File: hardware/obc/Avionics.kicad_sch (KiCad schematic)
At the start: 43 parts, among them J305 Conn_01x05, U103 RP2350_80QFN, Y101 Crystal_GND24_Small

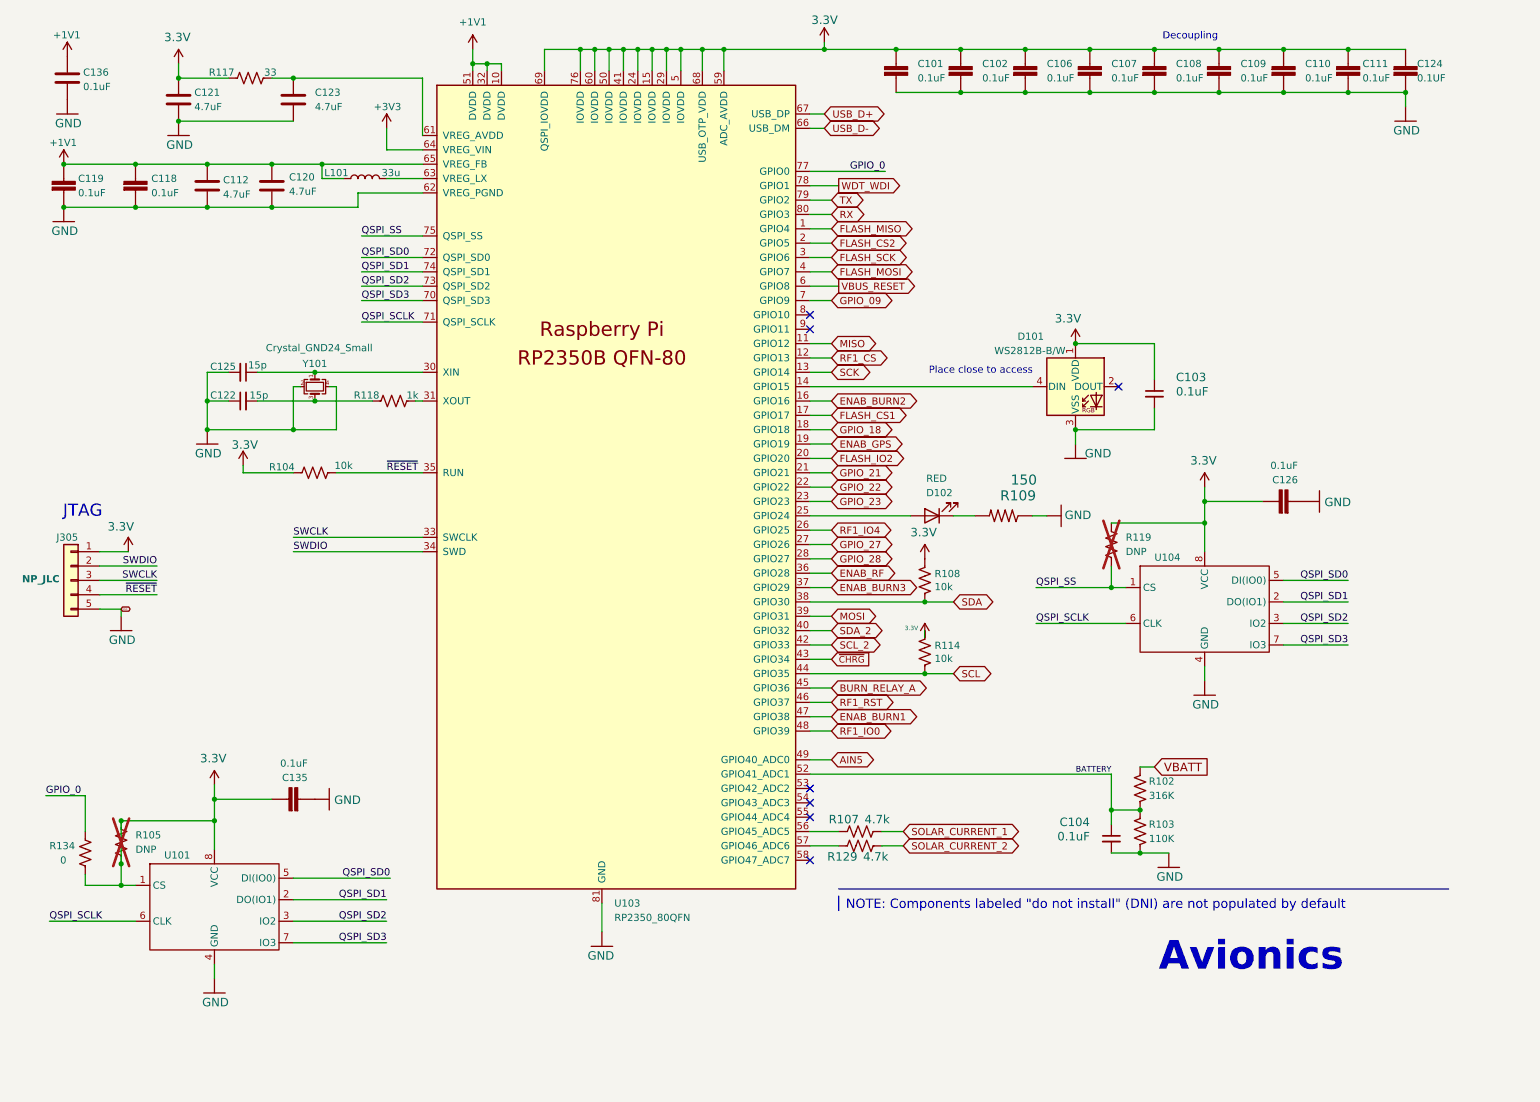
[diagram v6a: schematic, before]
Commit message: obc: Fixed errors from design review
- Gave proper attribution on all pages
- Spread out components on Avionics page
- Changed GPS power circuit
- Added a DNP resistor in between VBATT and VWATCHEDRAIL
- Added various other part numbers on Power Supervisor and Watch Dog Page
- Changed Power Supervisor and Watch Dog Page to page 3
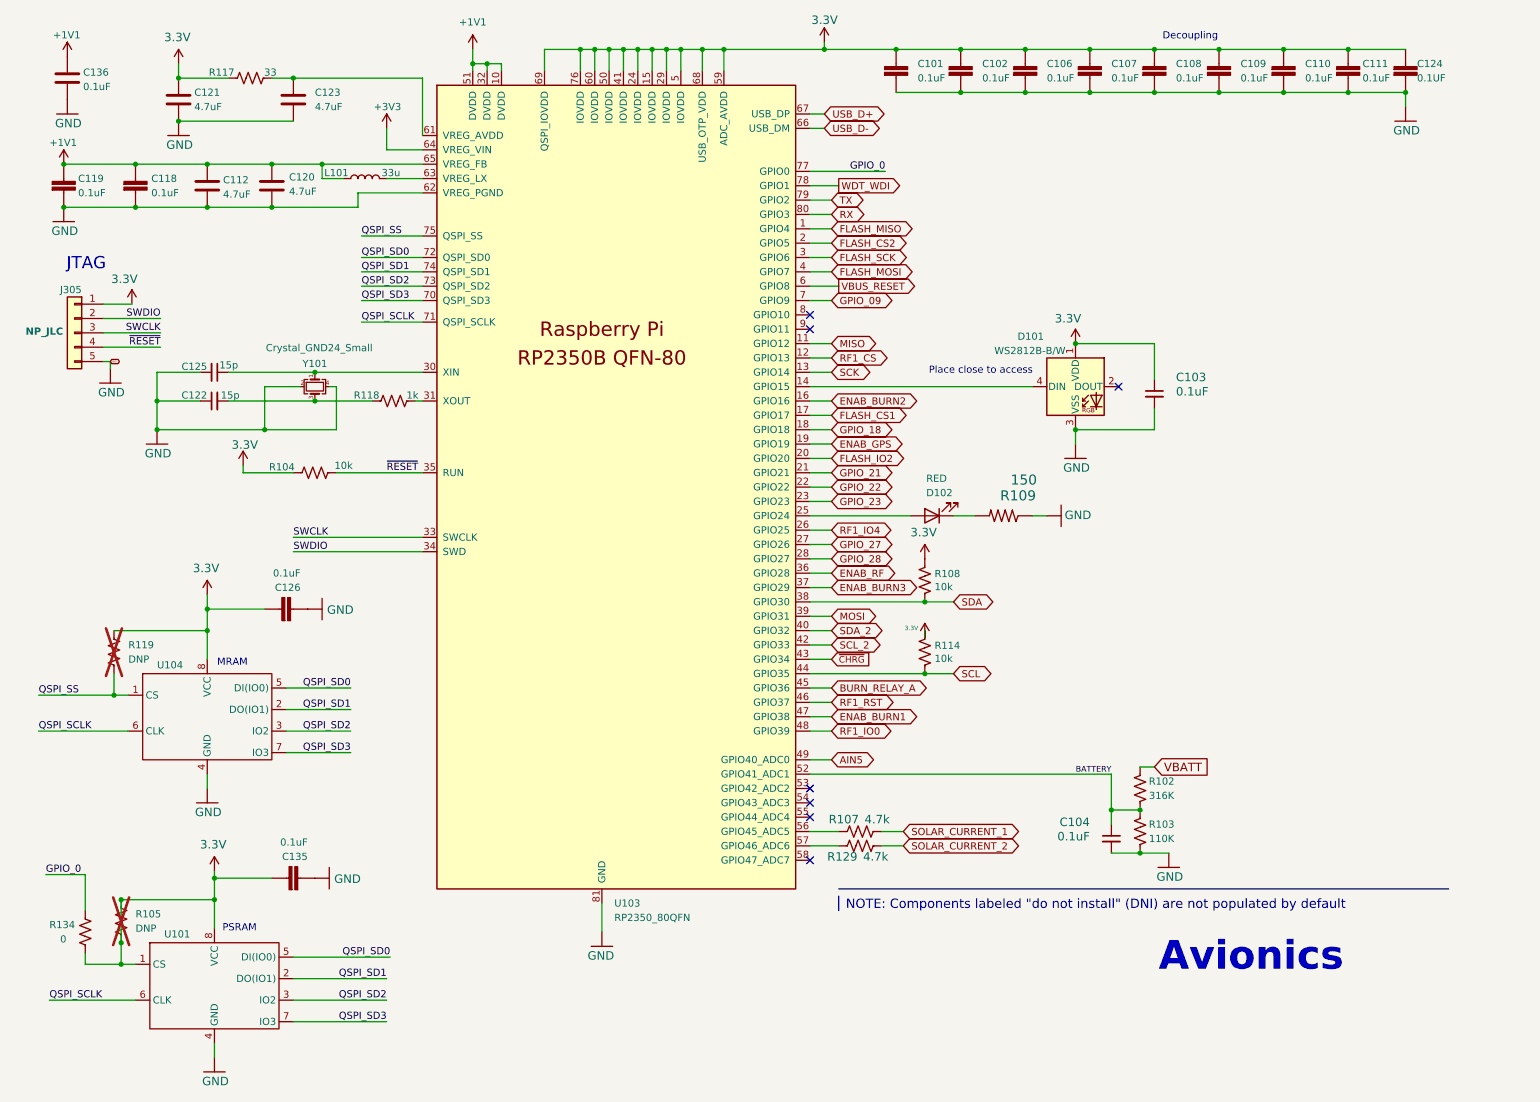
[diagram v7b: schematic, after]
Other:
- note added: "MRAM"
- note added: "PSRAM"
- company: Ruchir Kavulli, Michael Lyle -> Luke Titi, Ruchir Kavulli, Michael Lyle
- moved on the sheet: C122, C125, C126, C135, J305, R105, R119, R134, U101, U104

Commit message: obc: Fixed second design review, and fixed up BOM
- added layout comments on schematic
- fixed various comments
- added many LCSC # for components
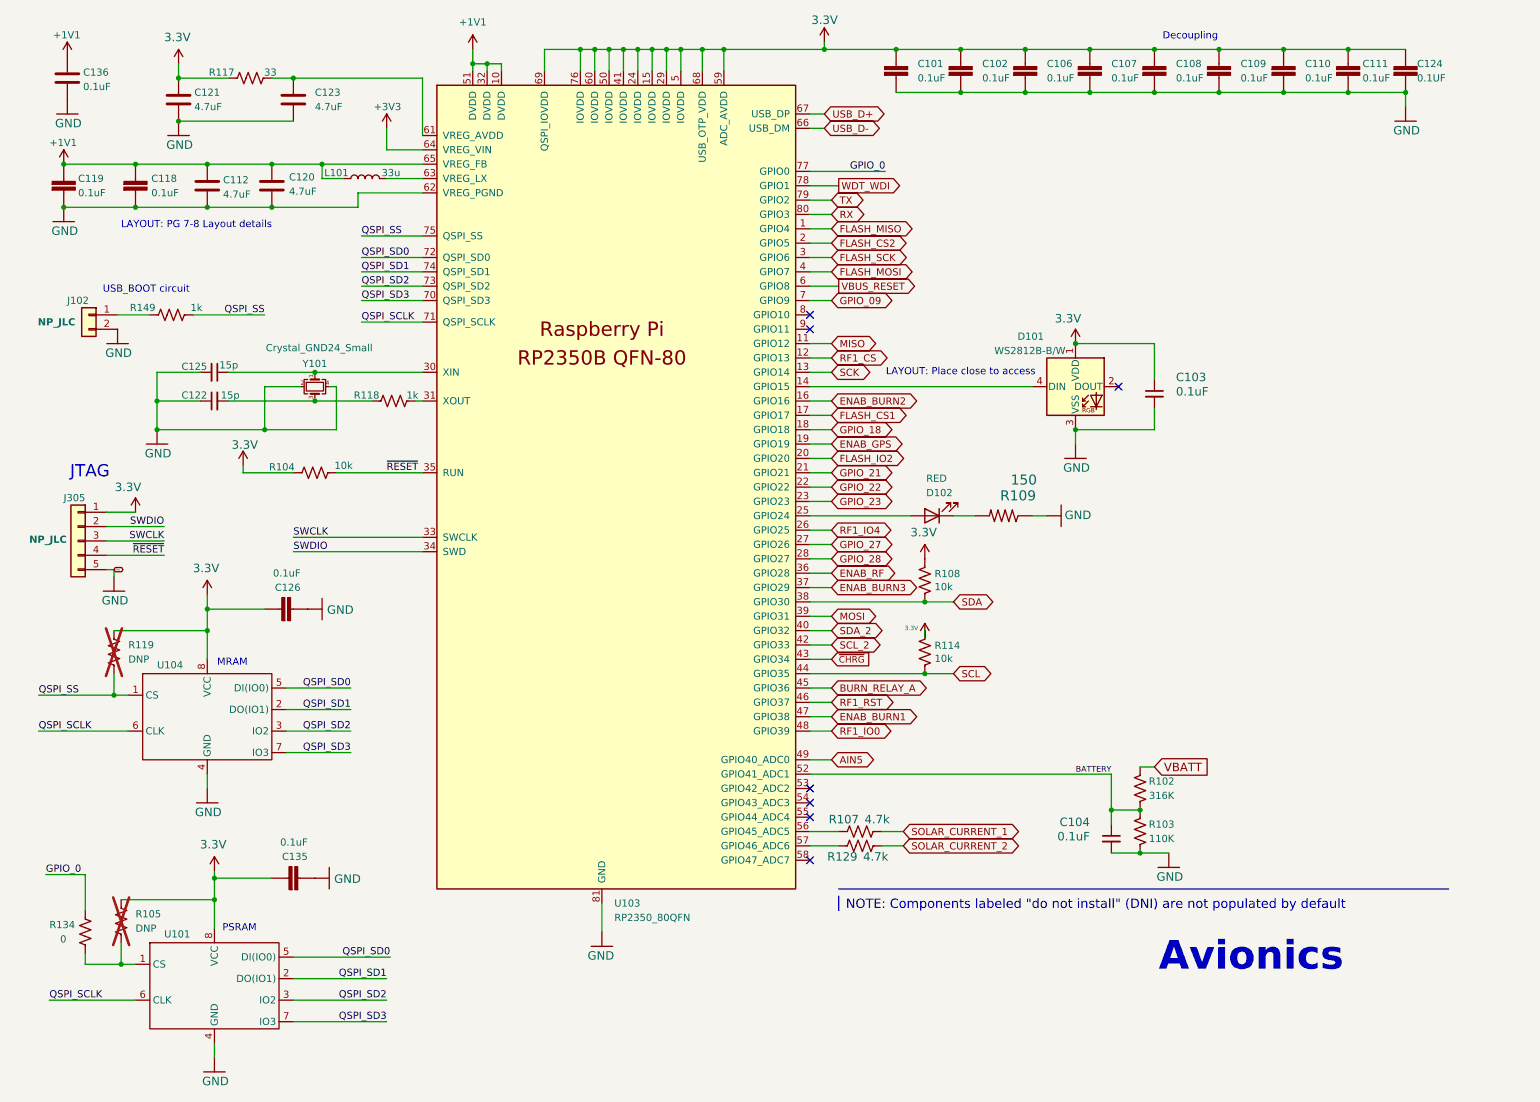
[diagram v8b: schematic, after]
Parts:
- added J102: Conn_01x05, Connector_PinHeader_2.00mm:PinHeader_1x02_P2.00mm_Vertical, symbol Connector_Generic:Conn_01x02
- added R149: 1k, Resistor_SMD:R_0603_1608Metric, symbol Device:R_US
- C101, C102, C106, C107, C108, C109, C110, C111, C118, C119, C124, C126, C135, C136: LCSC (none) -> C1591
- C112, C120, C121, C123: LCSC (none) -> C1705
- C122, C125: LCSC (none) -> C107037
- R117: LCSC (none) -> C108661
- R118: LCSC (none) -> C844746
- R134: footprint (none) -> Resistor_SMD:R_0603_1608Metric; LCSC (none) -> C100044
- Y101: LCSC (none) -> C20625731
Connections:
- net 3.3V: no longer R105.2, R134.2, U101.1 (CS)
- net GND: now also J102.2 (Pin_2)
- net QSPI_SS: now also R149.2
- new net: R105.2, R134.2, U101.1 (CS)
- new net: J102.1 (Pin_1), R149.1
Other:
- note added: "LAYOUT: PG 7-8 Layout details"
- note added: "LAYOUT: Place close to access"
- note added: "USB_BOOT circuit"
- note removed: "Place close to access"
- moved on the sheet: J305
